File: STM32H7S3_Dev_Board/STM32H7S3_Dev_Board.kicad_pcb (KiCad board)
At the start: 6 copper layers, 73 x 72 mm, 131 parts, among them J1 Conn_02x06_Odd_Even, J2 Conn_02x10_Odd_Even, J3 Conn_02x13_Odd_Even, J4 15910060, J5 Conn_02x07_Odd_Even, J6 Conn_02x04_Odd_Even, J7 Conn_01x02, J8 Conn_01x02, J9 UB1611-HGN, Q1 STD2805T4, Q2 STL40DN3LLH5, Q3 STL40DN3LLH5, SW1 SKRPABE010, SW2 SKRPABE010, SW3 SKRPABE010, SW4 SKRPABE010, U1 MX25UW25645GXDI00, U2 STM32H7S3Z8Tx, U3 ADAU1466WBCPZ300RL, U4 ADM811TARTZ, U5 AP7361EA-33E-13, U6 AP2127N-1.8TRG1, U7 TCPP03-M20, U8 ESDA25P35-1U1M, U9 ECMF2-40A100N6, X1 24MHz, X2 12.288MHz

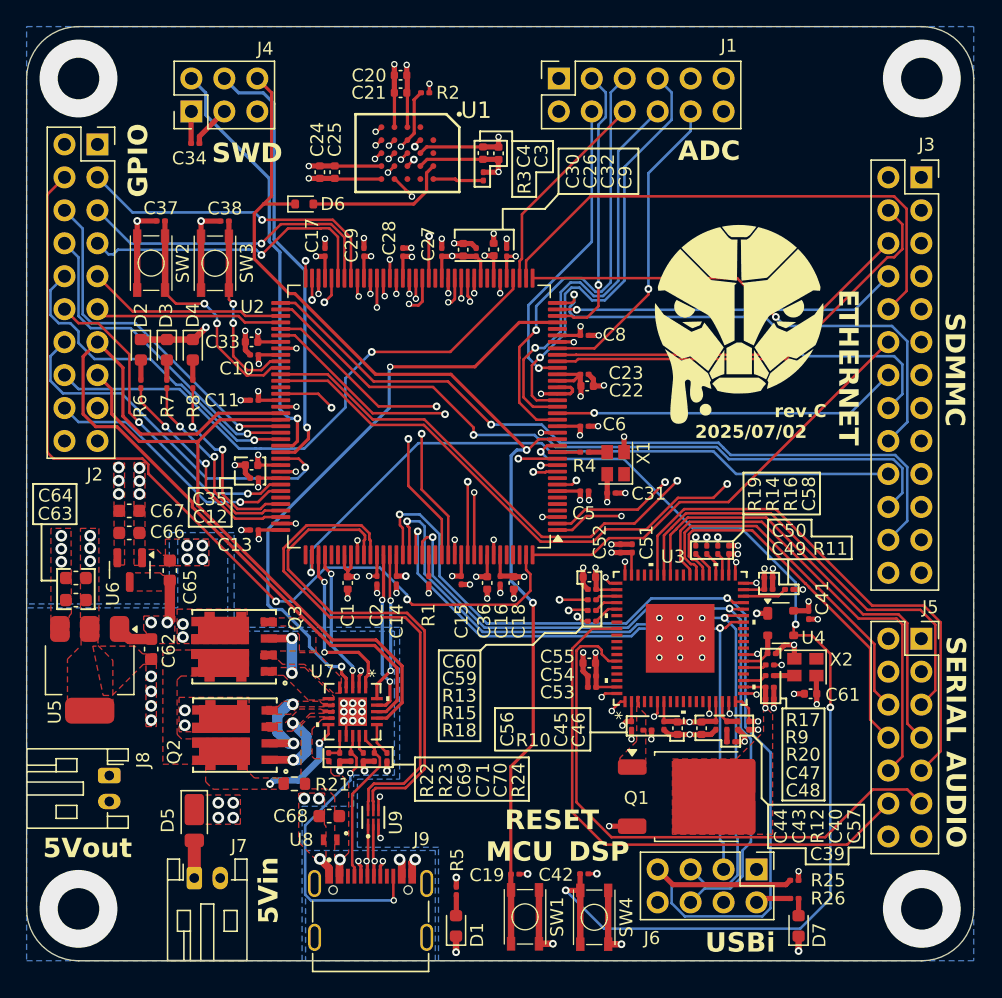
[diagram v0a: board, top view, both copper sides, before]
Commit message: Change the 3D model data path settings.
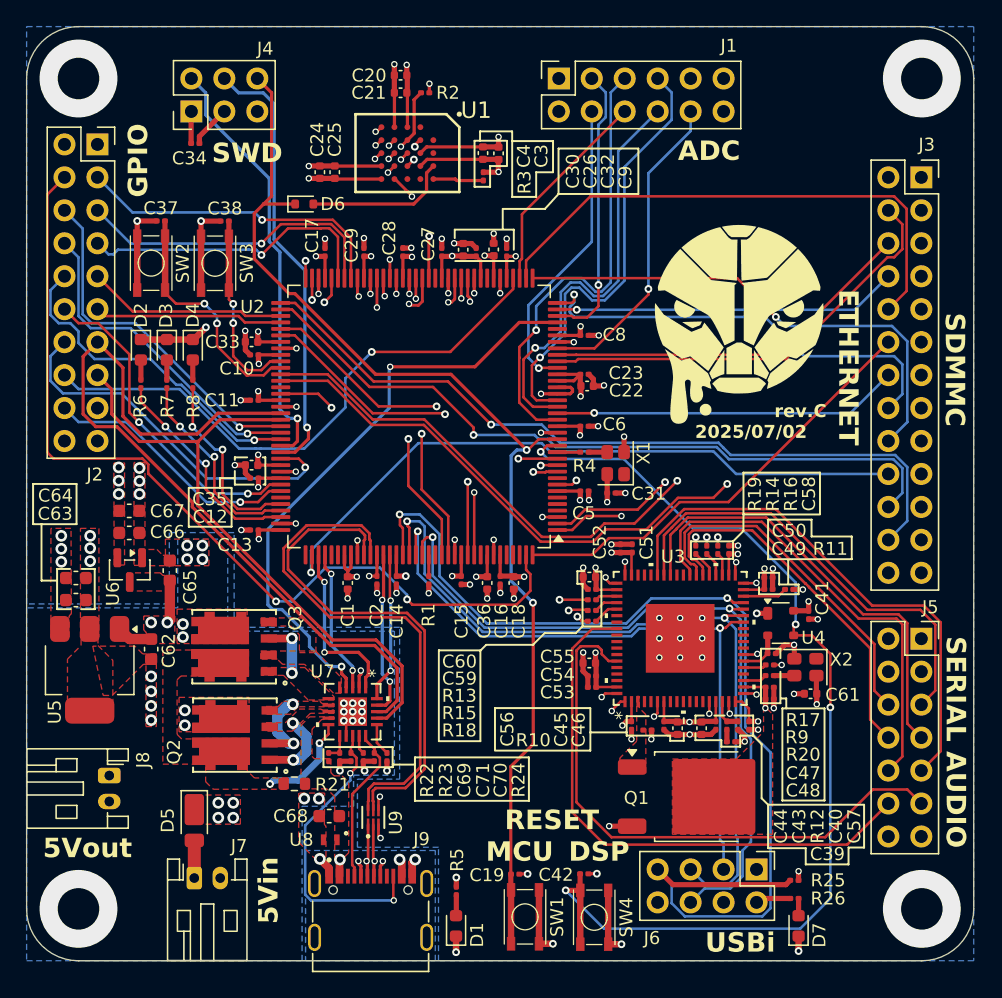
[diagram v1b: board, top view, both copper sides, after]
